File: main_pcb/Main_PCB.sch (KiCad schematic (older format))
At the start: 52 parts, among them J1 DBG, J2 UI, J3 UI, J4 Raspberry_Pi_Zero_WH, J5 UI, J6 UI, J7 UPDN, J8 ISP, Q1 BSS123, Q2 HSS2307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

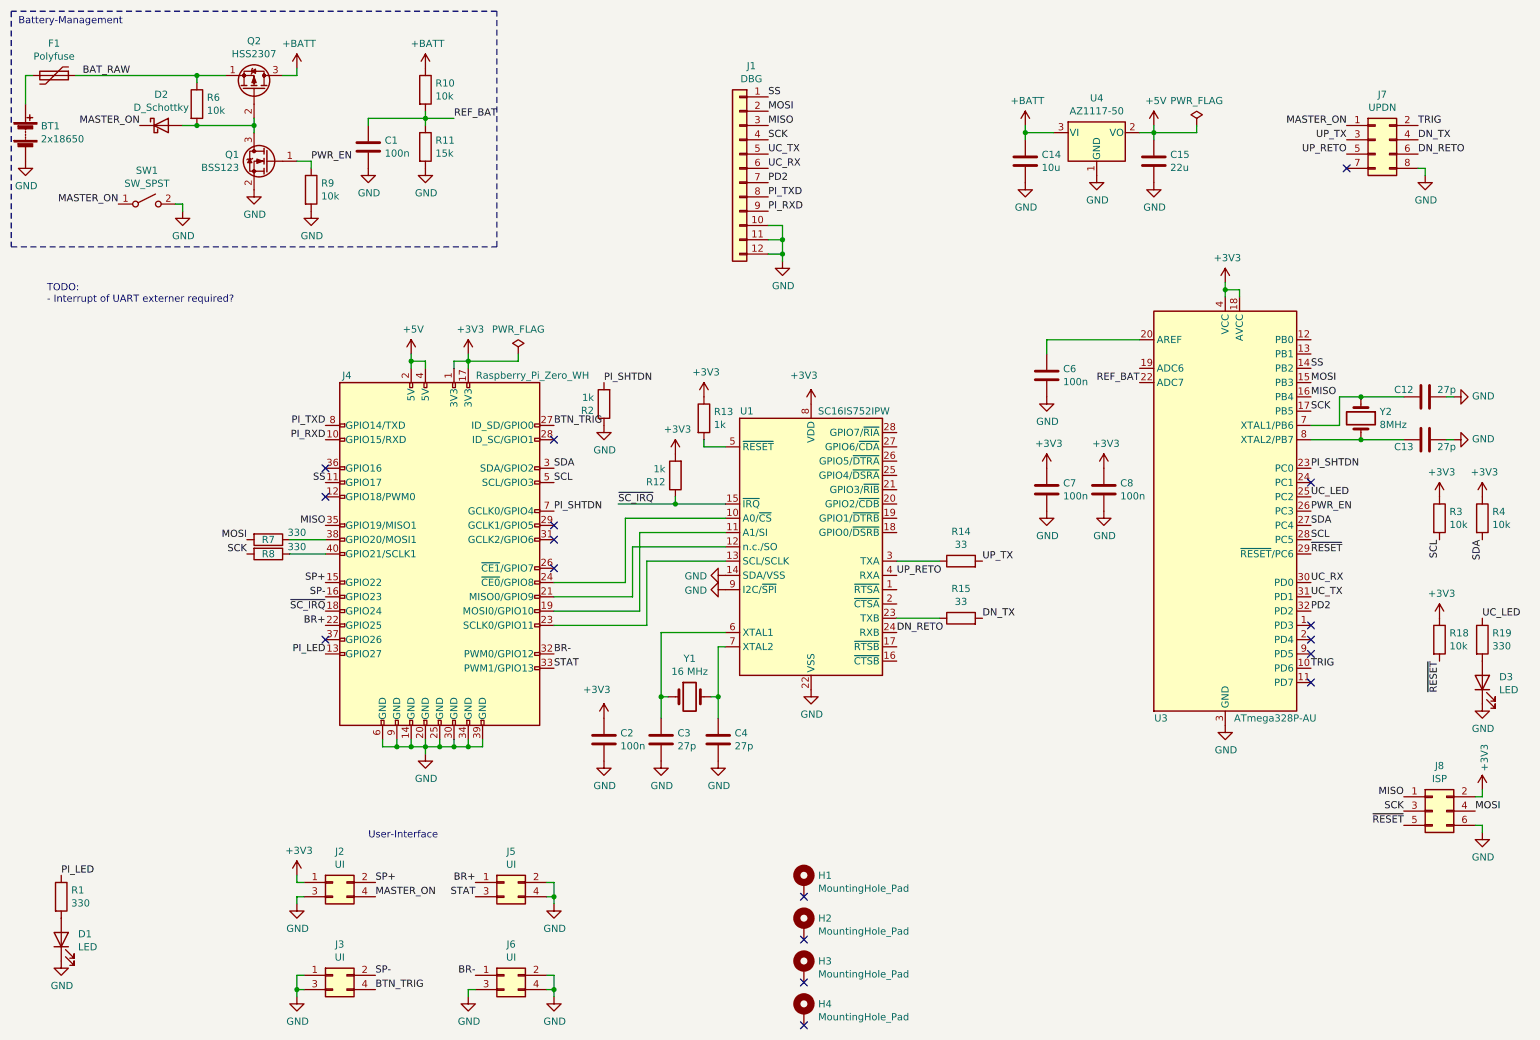
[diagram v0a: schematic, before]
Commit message: Minor fixes to make ERC happy (except one message which I don't understand)
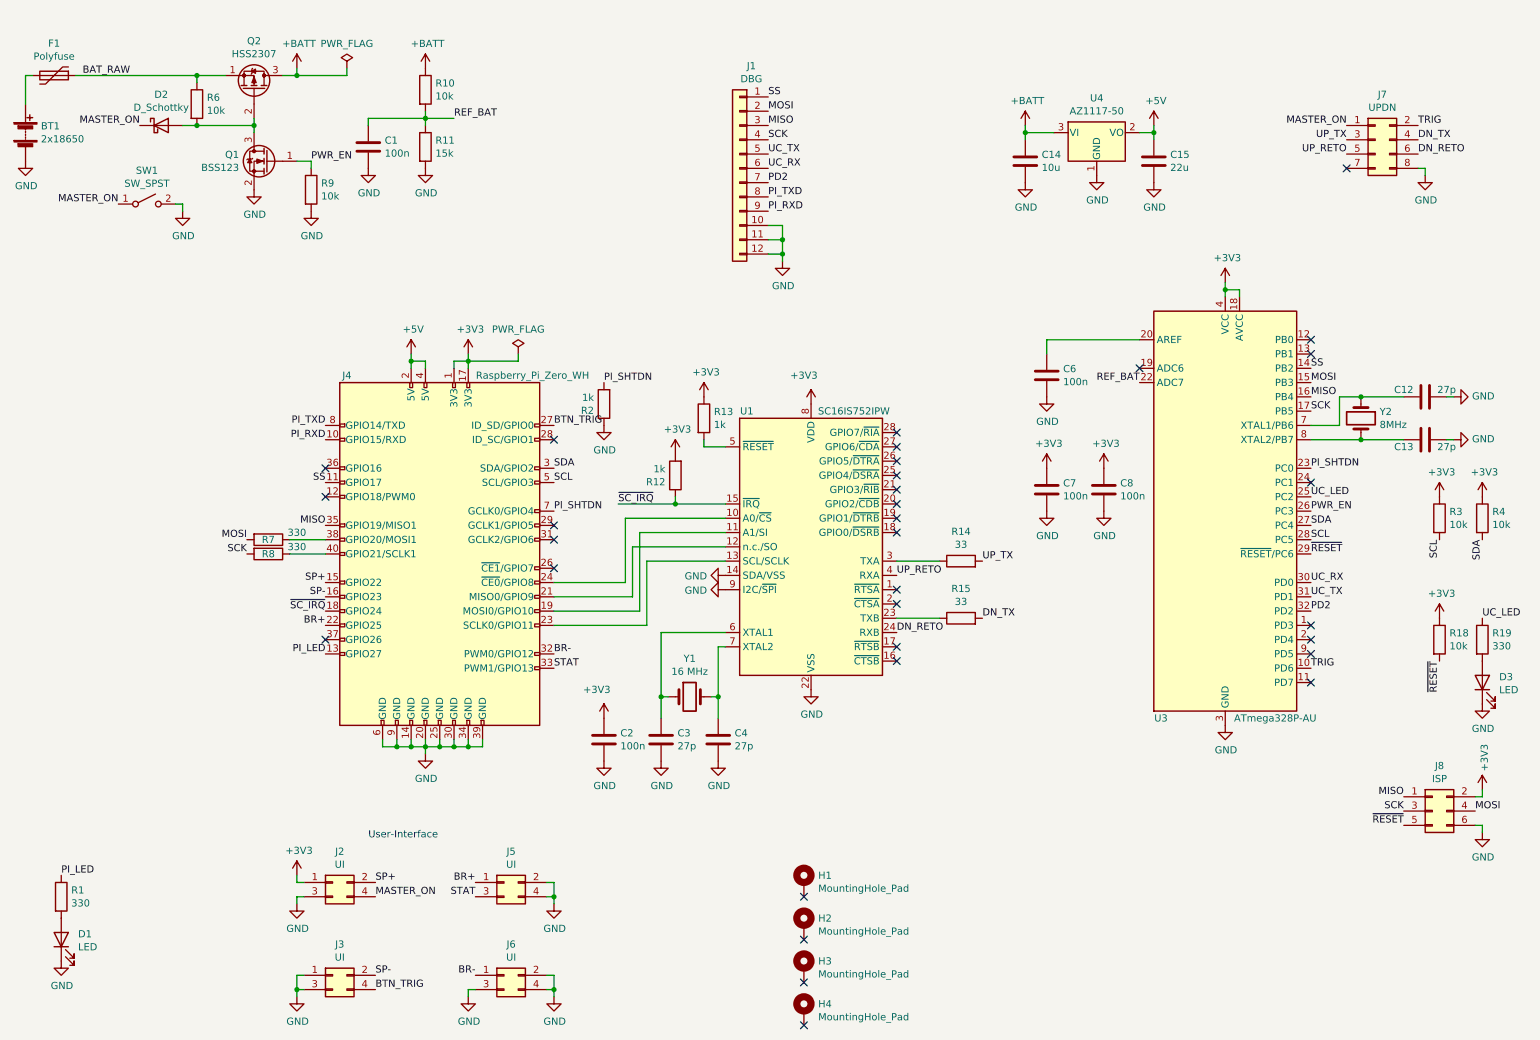
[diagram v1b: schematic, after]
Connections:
- no-connect marks 17 -> 32
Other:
- note removed: "Battery-Management"
- note removed: "TODO:\n- Interrupt of UART externer required?"

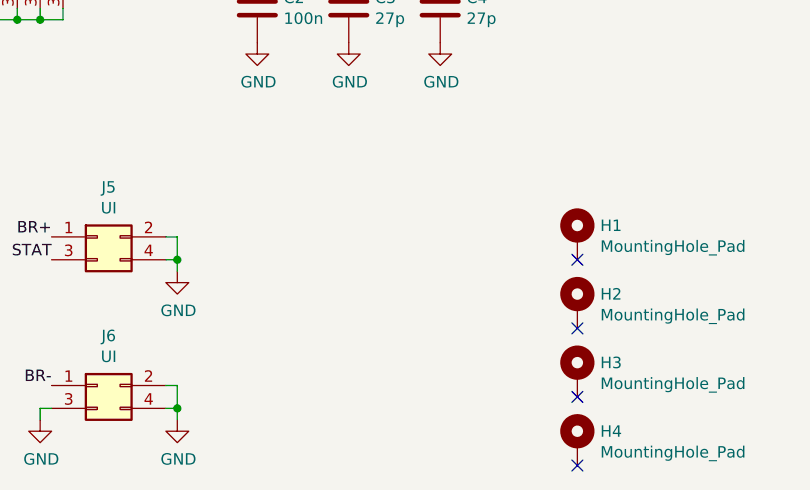
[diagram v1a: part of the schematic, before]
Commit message: Added pin header for ui trigger button for external trigger button
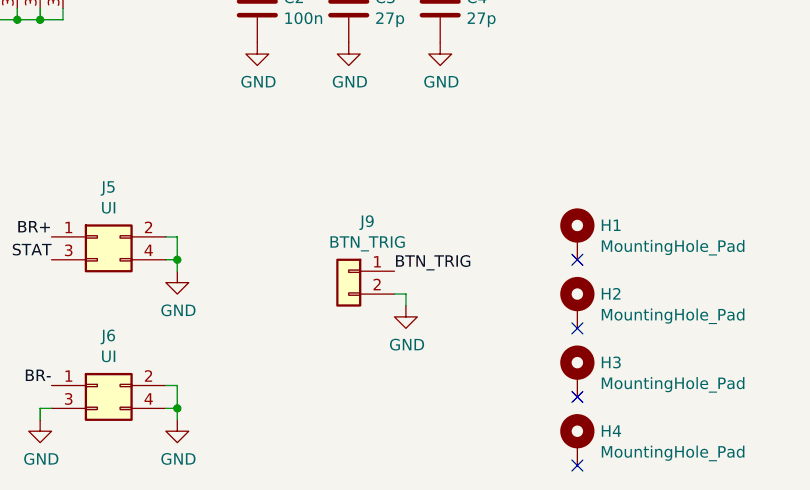
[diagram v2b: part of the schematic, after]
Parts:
- added J9: BTN_TRIG, Connector_PinHeader_2.54mm:PinHeader_1x02_P2.54mm_Vertical, symbol Connector_Generic:Conn_01x02
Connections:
- net BTN_TRIG: now also J9.1 (Pin_1)
- net GND: now also J9.2 (Pin_2)
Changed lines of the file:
@@
 NoConn ~ 9650 2900
 NoConn ~ 8450 3000
+Text Label 5300 6750 0    50   ~ 0
+BTN_TRIG
+$Comp
+L Connector_Generic:Conn_01x02 J9
+U 1 1 6185D43E
+P 5100 6750
+F 0 "J9" H 5018 6967 50  0000 C CNN
+F 1 "BTN_TRIG" H 5018 6876 50  0000 C CNN
+F 2 "Connector_PinHeader_2.54mm:PinHeader_1x02_P2.54mm_Vertical" H 5100 6750 50  0001 C CNN
+F 3 "~" H 5100 6750 50  0001 C CNN
+	1    5100 6750
+	-1   0    0    -1
+$EndComp
+$Comp
+L power:GND #PWR04
+U 1 1 6185E109
+P 5350 6900
+F 0 "#PWR04" H 5350 6650 50  0001 C CNN
+F 1 "GND" H 5355 6727 50  0000 C CNN
+F 2 "" H 5350 6900 50  0001 C CNN
+F 3 "" H 5350 6900 50  0001 C CNN
+	1    5350 6900
+	1    0    0    -1
+$EndComp
+Wire Wire Line
+	5300 6850 5350 6850
+Wire Wire Line
+	5350 6850 5350 6900
 $EndSCHEMATC

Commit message: output
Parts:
- J9: MPN (none) -> DNP
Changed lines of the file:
@@
 F 2 "Connector_PinHeader_2.54mm:PinHeader_1x02_P2.54mm_Vertical" H 5100 6750 50  0001 C CNN
 F 3 "~" H 5100 6750 50  0001 C CNN
+F 4 "DNP" H 5100 6750 50  0001 C CNN "MPN"
+F 5 "~" H 5100 6750 50  0001 C CNN "Manufacturer"
 	1    5100 6750
 	-1   0    0    -1
